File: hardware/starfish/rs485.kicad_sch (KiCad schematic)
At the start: 4 parts, among them J801 Feeders, U801 MAX3078E

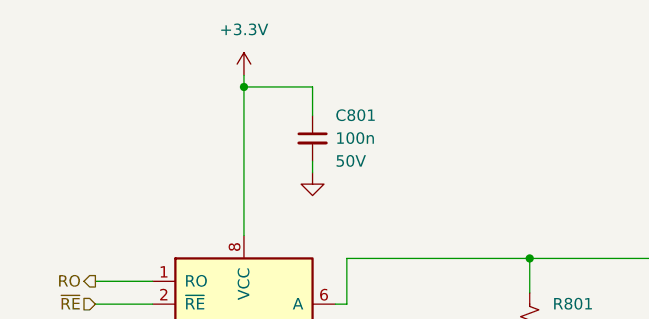
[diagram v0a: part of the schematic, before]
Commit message: Mostly finished starfish schematic, ready for layout!
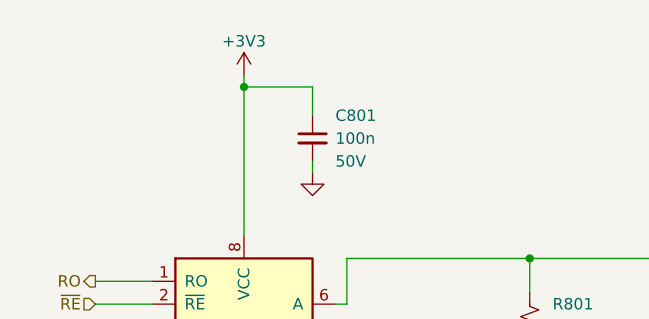
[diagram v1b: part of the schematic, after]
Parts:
- C801: footprint (none) -> winterbloom:C_0603_HandSolder; mpn (none) -> CL10B104KB8NNWC
- R801: footprint (none) -> winterbloom:R_0402_HandSolder
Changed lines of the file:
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@@
       (effects (font (size 1.27 1.27)) (justify left))
     )
-    (property "Footprint" "" (id 2) (at 144.526 106.934 90)
+    (property "Footprint" "winterbloom:R_0402_HandSolder" (id 2) (at 144.526 106.934 90)
       (effects (font (size 1.27 1.27)) hide)
     )
@@
     (pin "6")
   )
-  (symbol (lib_id "power:+3.3V") (at 111.76 78.74 0) (unit 1)
-    (in_bom yes) (on_board yes) (fields_autoplaced)
-    (property "Reference" "#PWR0801" (id 0) (at 111.76 82.55 0)
-      (effects (font (size 1.27 1.27)) hide)
-    )
-    (property "Value" "+3.3V" (id 1) (at 111.76 73.66 0))
-    (property "Footprint" "" (id 2) (at 111.76 78.74 0)
-      (effects (font (size 1.27 1.27)) hide)
-    )
-    (property "Datasheet" "" (id 3) (at 111.76 78.74 0)
-      (effects (font (size 1.27 1.27)) hide)
-    )
-    (pin "1")
-  )
   (symbol (lib_id "power:GND") (at 111.76 116.84 0) (unit 1)
     (in_bom yes) (on_board yes)
@@
       (effects (font (size 1.27 1.27)) (justify left))
     )
-    (property "Footprint" "" (id 2) (at 119.38 85.725 0)
+    (property "Footprint" "winterbloom:C_0603_HandSolder" (id 2) (at 119.38 85.725 0)
       (effects (font (size 1.27 1.27)) hide)
     )
-    (property "Datasheet" "" (id 3) (at 119.38 85.725 0)
+    (property "Datasheet" "~" (id 3) (at 119.38 85.725 0)
       (effects (font (size 1.27 1.27)) hide)
     )
     (property "Rating" "50V" (id 4) (at 121.92 88.2712 0)
       (effects (font (size 1.27 1.27)) (justify left))
+    )
+    (property "mpn" "CL10B104KB8NNWC" (id 5) (at 119.38 85.725 0)
+      (effects (font (size 1.27 1.27)) hide)
     )
     (pin "1")
@@
       (effects (font (size 1.27 1.27)) hide)
     )
+    (pin "1")
+  )
+  (symbol (lib_id "power:+3V3") (at 111.76 78.74 0) (unit 1)
+    (in_bom yes) (on_board yes)
+    (property "Reference" "#PWR0801" (id 0) (at 111.76 82.55 0)
+      (effects (font (size 1.27 1.27)) hide)
+    )
+    (property "Value" "+3V3" (id 1) (at 111.76 74.93 0))
+    (property "Footprint" "" (id 2) (at 111.76 78.74 0)
+      (effects (font (size 1.27 1.27)) hide)
+    )
+    (property "Datasheet" "" (id 3) (at 111.76 78.74 0)
+      (effects (font (size 1.27 1.27)) hide)
+    )

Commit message: Run through purchasing, update some cap sizes
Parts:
- R801: mpn (none) -> CRGCQ0402F120R
- U801: mpn MAX3078EASA+-ND -> MAX3078EESA
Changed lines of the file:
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@@
       (effects (font (size 1.27 1.27)) (justify left))
+    )
+    (property "mpn" "CRGCQ0402F120R" (id 5) (at 143.51 106.68 0)
+      (effects (font (size 1.27 1.27)) hide)
     )
     (pin "1")
@@
       (effects (font (size 1.27 1.27)) hide)
     )
-    (property "mpn" "MAX3078EASA+-ND" (id 7) (at 111.76 106.68 0)
+    (property "mpn" "MAX3078EESA" (id 7) (at 111.76 106.68 0)
       (effects (font (size 1.27 1.27)) hide)
     )
